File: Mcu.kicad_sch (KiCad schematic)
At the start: 19 parts, among them U7 STM32H723VGHx, X2 X322516MLB4SI

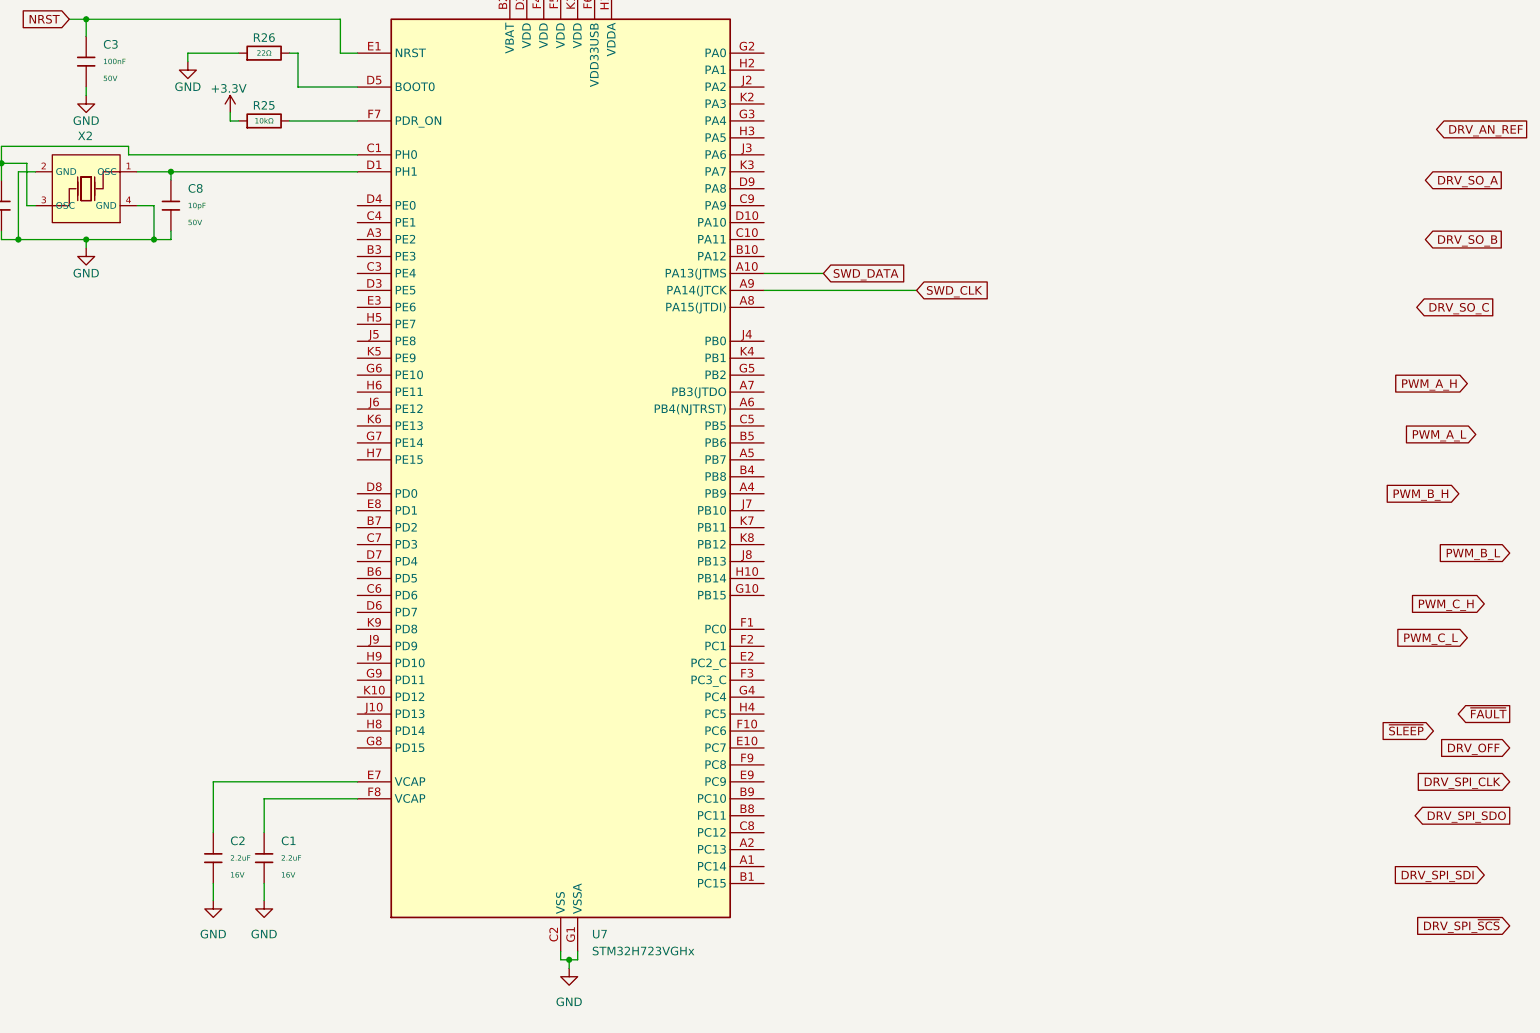
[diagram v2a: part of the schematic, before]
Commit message: Add encoder sheet
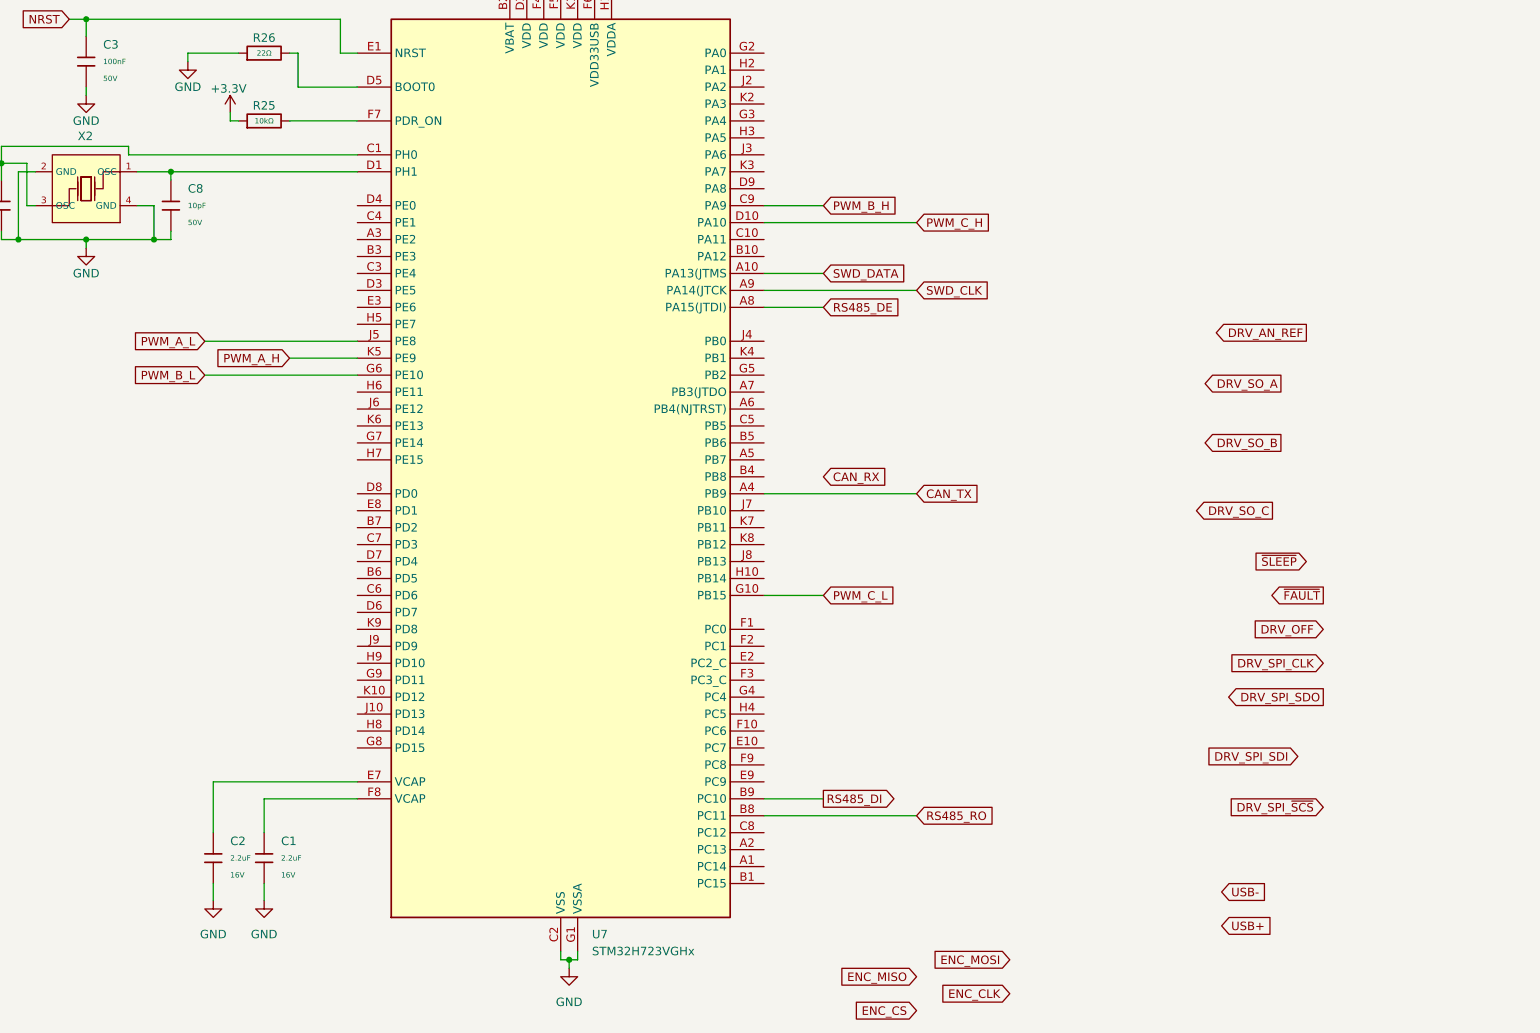
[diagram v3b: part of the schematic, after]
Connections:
- net PWM_A_H: now also U7.K5 (PE9)
- net PWM_A_L: now also U7.J5 (PE8)
- net PWM_B_H: now also U7.C9 (PA9)
- net PWM_B_L: now also U7.G6 (PE10)
- net PWM_C_H: now also U7.D10 (PA10)
- net PWM_C_L: now also U7.G10 (PB15)
- net CAN_TX: now reaches U7.A4 (PB9)
- net RS485_DE: now reaches U7.A8 (PA15(JTDI))
- net RS485_RO: now reaches U7.B8 (PC11)
- net RS485_DI: now reaches U7.B9 (PC10)

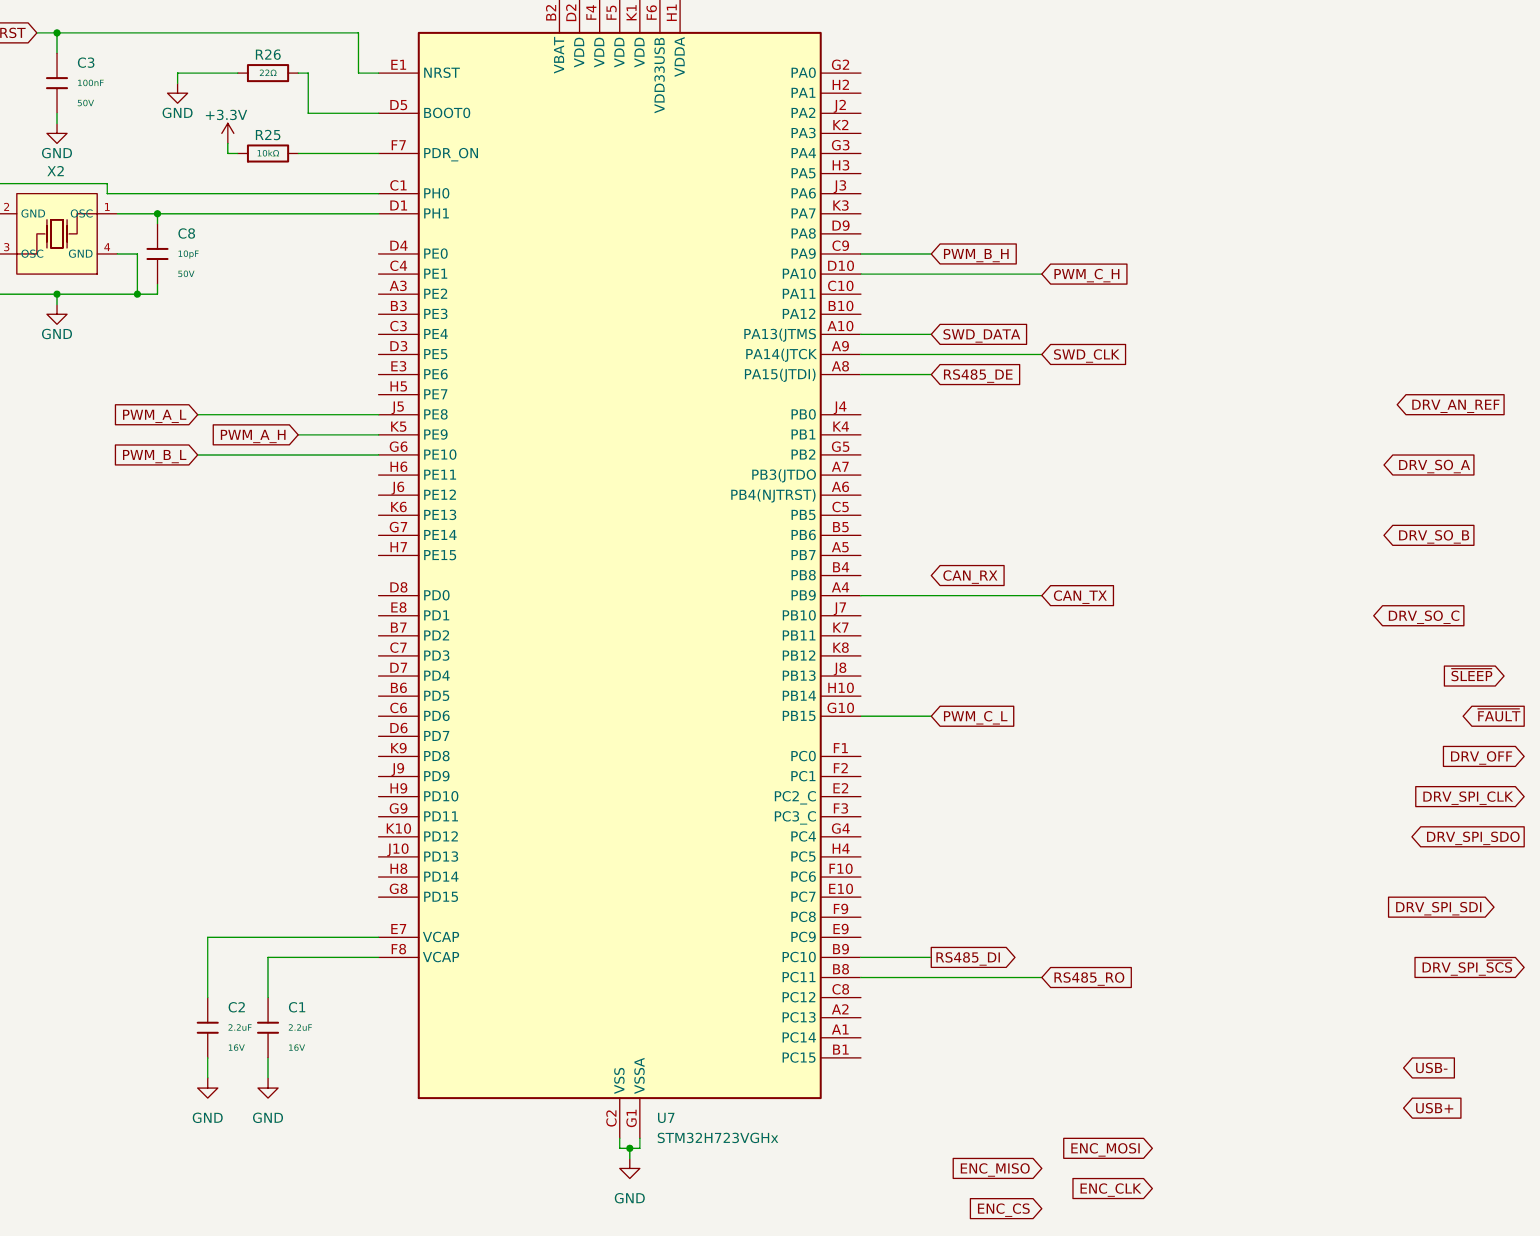
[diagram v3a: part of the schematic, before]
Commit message: Add mcu connections
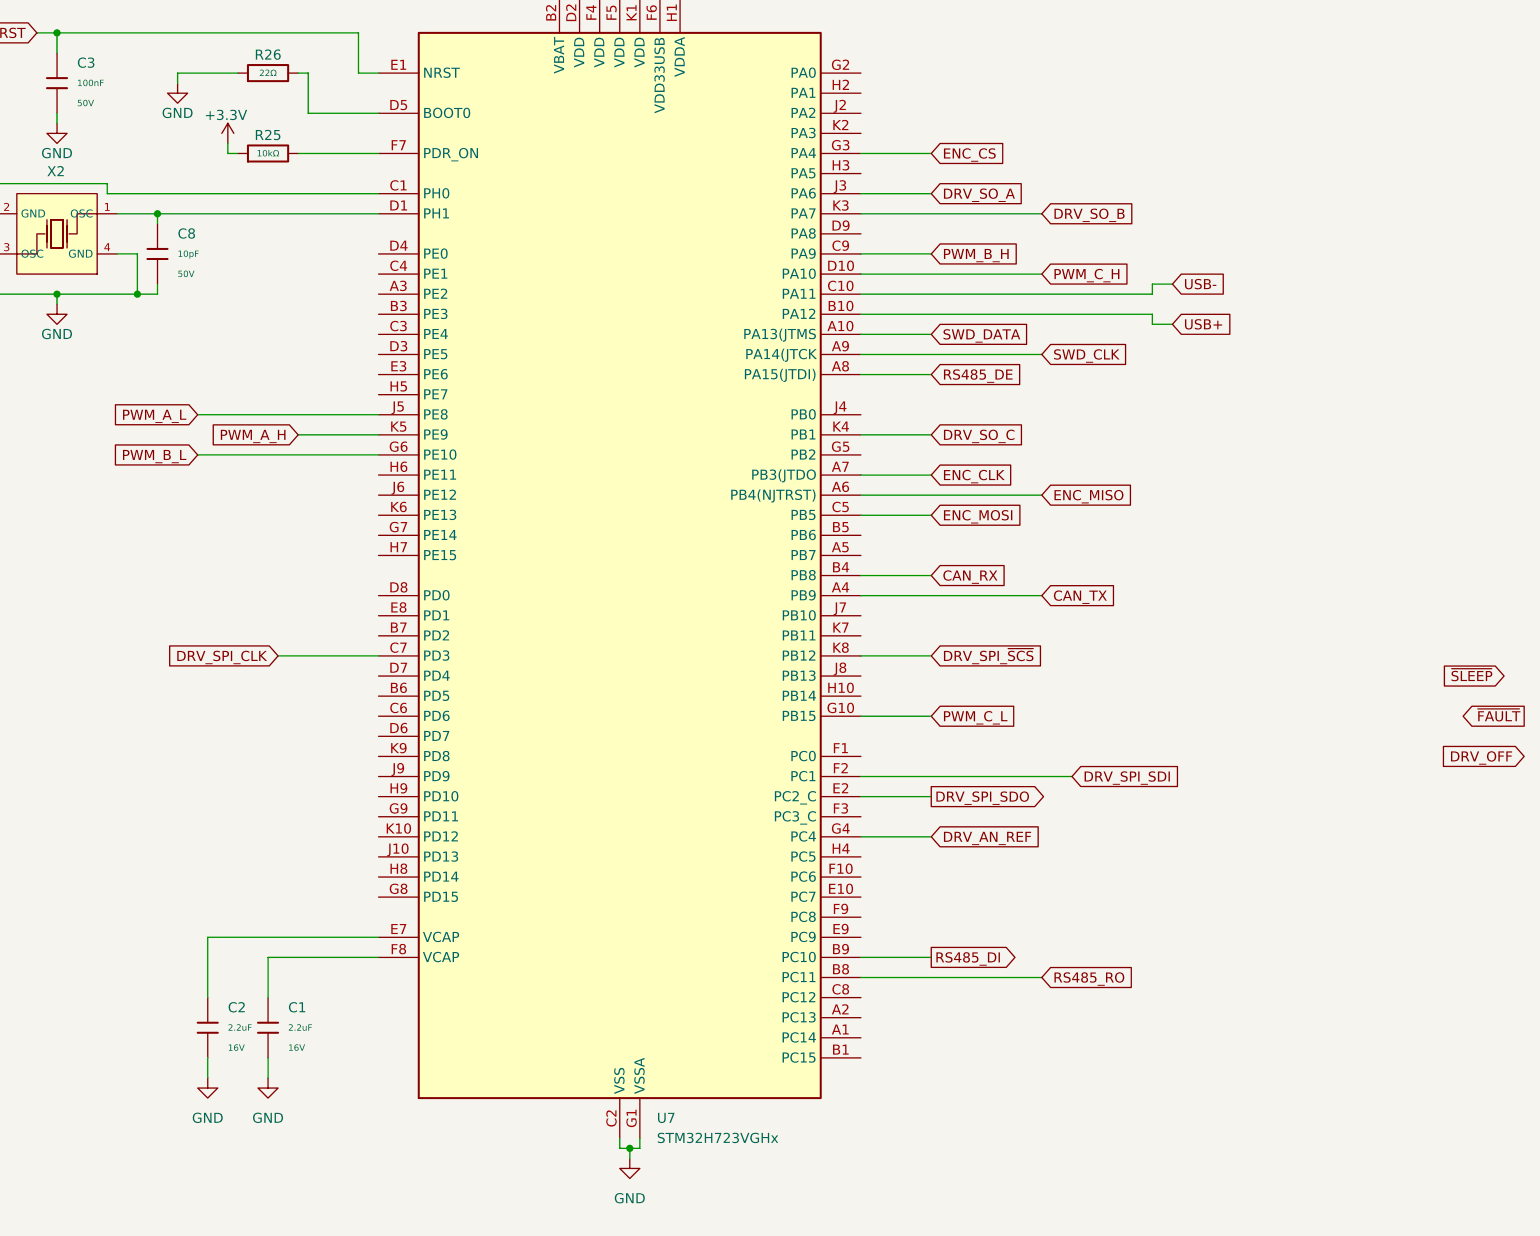
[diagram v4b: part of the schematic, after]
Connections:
- net CAN_RX: now also U7.B4 (PB8)
- net DRV_AN_REF: now also U7.G4 (PC4)
- net DRV_SO_A: now also U7.J3 (PA6)
- net DRV_SO_B: now also U7.K3 (PA7)
- net DRV_SO_C: now also U7.K4 (PB1)
- net DRV_SPI_CLK: now also U7.C7 (PD3)
- net DRV_SPI_SDI: now also U7.F2 (PC1)
- net DRV_SPI_SDO: now also U7.E2 (PC2_C)
- net DRV_SPI_~{SCS}: now also U7.K8 (PB12)
- net ENC_CLK: now also U7.A7 (PB3(JTDO)
- net ENC_CS: now also U7.G3 (PA4)
- net ENC_MISO: now also U7.A6 (PB4(NJTRST))
- net ENC_MOSI: now also U7.C5 (PB5)
- net USB+: now also U7.B10 (PA12)
- net USB-: now also U7.C10 (PA11)

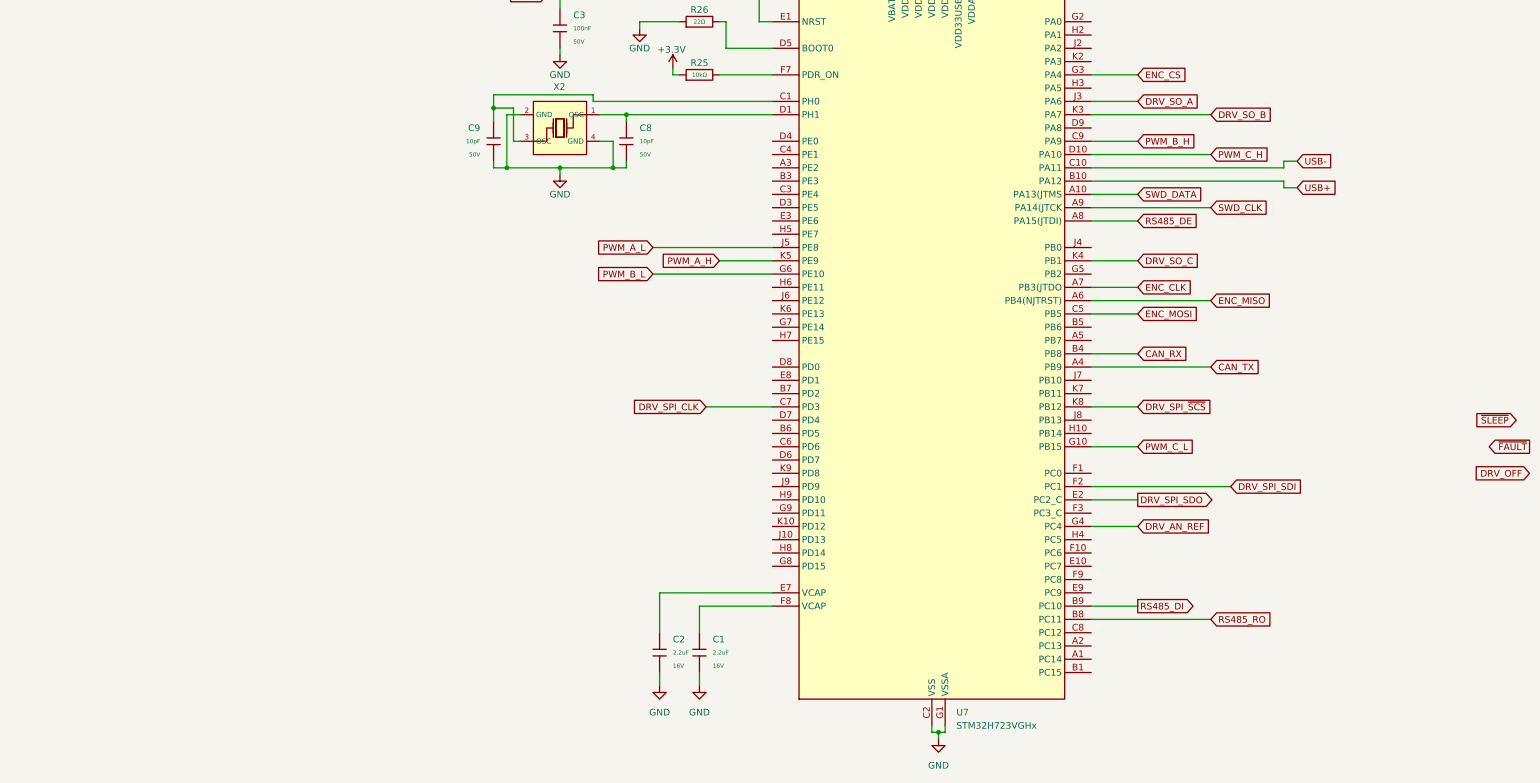
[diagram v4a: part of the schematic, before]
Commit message: Added DRV layout
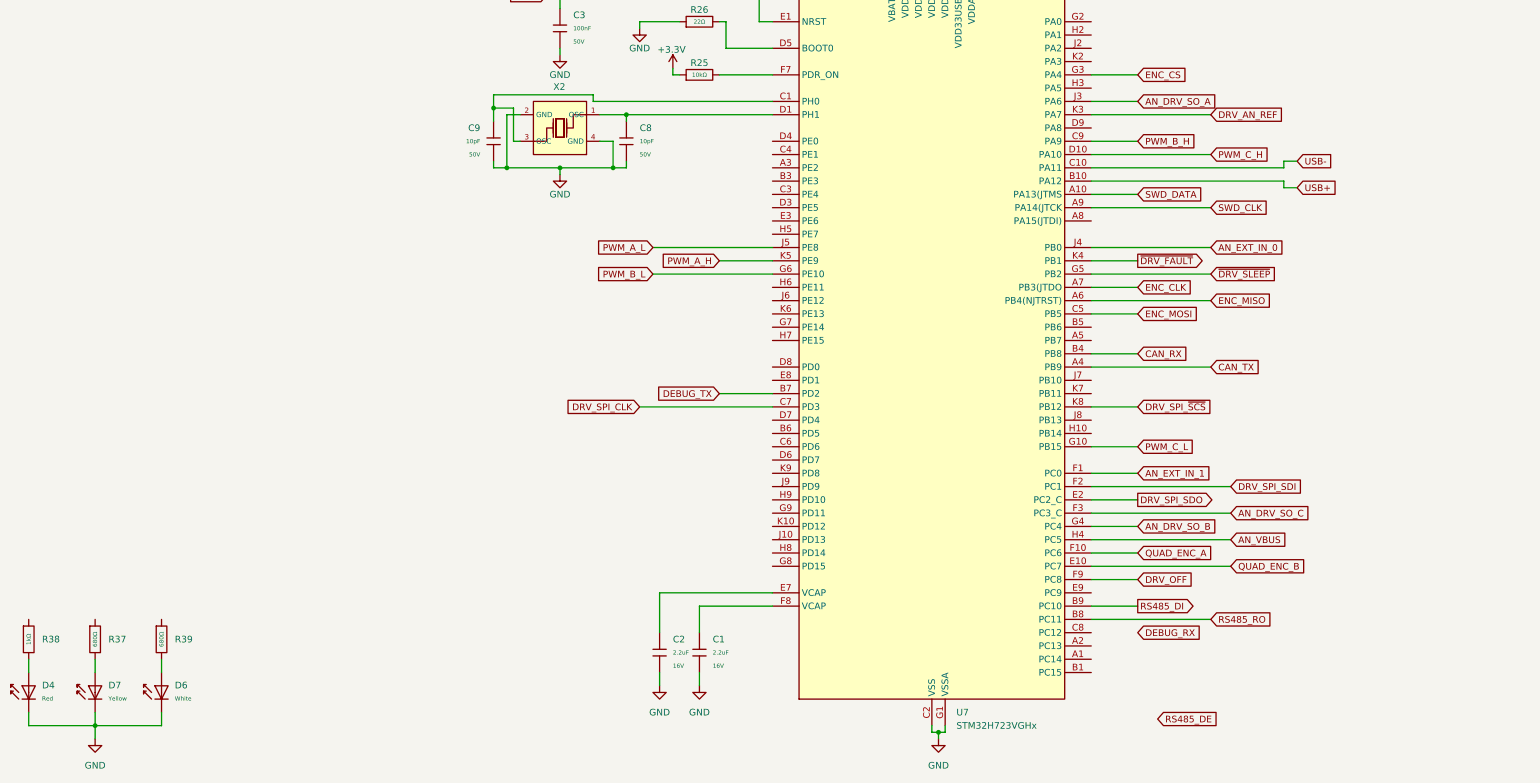
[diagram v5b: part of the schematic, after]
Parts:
- added D4: Red, PCM_JLCPCB:D_0603, symbol PCM_JLCPCB-Diodes:LED,0603,Red
- added D6: White, PCM_JLCPCB:D_0603, symbol PCM_JLCPCB-Diodes:LED,0603,White
- added D7: Yellow, PCM_JLCPCB:D_0603, symbol PCM_JLCPCB-Diodes:LED,0603,Yellow
- added R37, R39: 680Ω, PCM_JLCPCB:R_0603, symbol PCM_JLCPCB-Resistors:0603,680Ω
- added R38: 1kΩ, PCM_JLCPCB:R_0603, symbol PCM_JLCPCB-Resistors:0603,1kΩ
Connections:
- net DRV_SO_B is gone; now on net DRV_AN_REF: U7.K3 (PA7)
- net DRV_AN_REF: no longer U7.G4 (PC4)
- net DRV_OFF: now also U7.F9 (PC8)
- net GND: now also D4.1, D6.1, D7.1
- net RS485_DE: no longer U7.A8 (PA15(JTDI))
- net DEBUG_TX: now reaches U7.B7 (PD2)
- net QUAD_ENC_B: now reaches U7.E10 (PC7)
- net AN_EXT_IN_1: now reaches U7.F1 (PC0)
- net QUAD_ENC_A: now reaches U7.F10 (PC6)
- net AN_DRV_SO_C: now reaches U7.F3 (PC3_C)
- net ~{DRV_SLEEP}: now reaches U7.G5 (PB2)
- net AN_VBUS: now reaches U7.H4 (PC5)
- net AN_EXT_IN_0: now reaches U7.J4 (PB0)
- net DRV_SO_A renamed AN_DRV_SO_A
- net DRV_SO_C renamed ~{DRV_FAULT}
- new net: D4.2, R38.2
- new net: D7.2, R37.2
- new net: D6.2, R39.2
- new net AN_DRV_SO_B: U7.G4 (PC4)
